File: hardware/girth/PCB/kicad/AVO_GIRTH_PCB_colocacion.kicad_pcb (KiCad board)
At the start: 4 copper layers, 65.5 x 43.5 mm, 122 parts, among them J1 USB-C 16P, J2 BATERÍA 1S, K1 G6KU-2F-Y DC3, Q1 AO3401A, Q10 AO3401A, Q11 AO3400A, Q12 2N7002, Q13 AO3400A, Q14 AO3401A, Q15 2N7002, Q16 2N7002, Q17 AO3401A, Q18 2N7002, Q2 AO3401A, Q3 AO3401A, SW1 REED (1), SW2 REED (2), U1 BQ51013BRHLR, U2 BQ24072RGTR, U3 RT9080-33GJ5, U4 ESP32-C6-MINI-1U-N4, U5 BNO085, U6 USBLC6-2SC6, Y1 32,768 kHz 12,5 pF

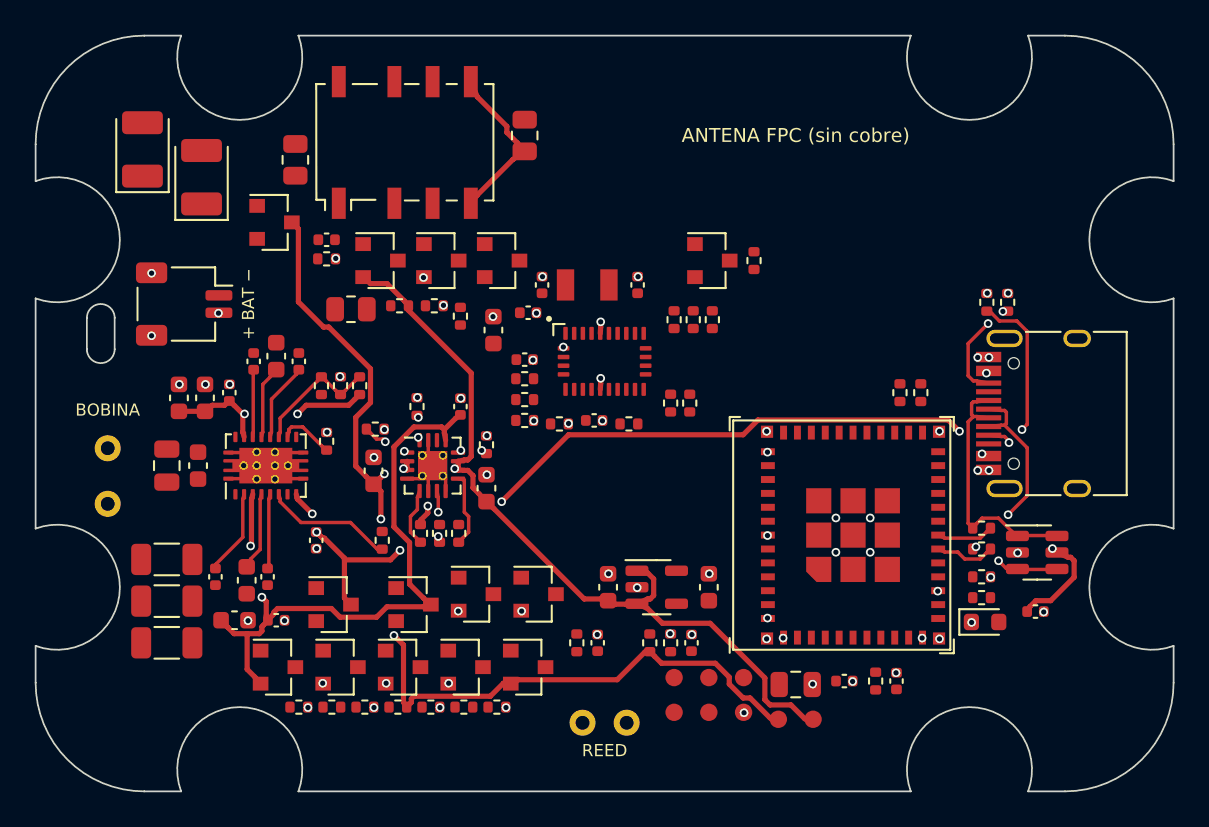
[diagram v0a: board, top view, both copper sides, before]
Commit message: PCB cincha REV B: ESP32-C3-MINI-1U-N4, LSM6DS3TR-C + MMC5983MA por I²C, corte de batería con MOSFET; REV A (C6) congelada
- REV A copiada tal cual a hardware/girth/PCB_REV_A_C6 (puerta superada en e9e5166).
- U4 ESP32-C3-MINI-1U-N4 (C2911374, 1191 uds. en JLCPCB el 2026-10-29); nueva asignación de GPIO.
- IMU: BNO085 (19,50 US$, 80 uds.) sustituido por LSM6DS3TR-C + MMC5983MA (I²C), mismos datos de 9 ejes.
- Relé biestable sustituido por enclavamiento PMOS/NMOS (reed por flanco, 5 V de carga, PWR_HOLD).
- R6/R7 a 3k3 (piezas Basic). Ficheros de fabricación con nombres C3.

Co-Authored-By: Claude Opus 5.5 <noreply@anthropic.com>
Claude-Session: https://claude.ai/code/session_01CHDvF8BfHwPLkrFs9S3ECm
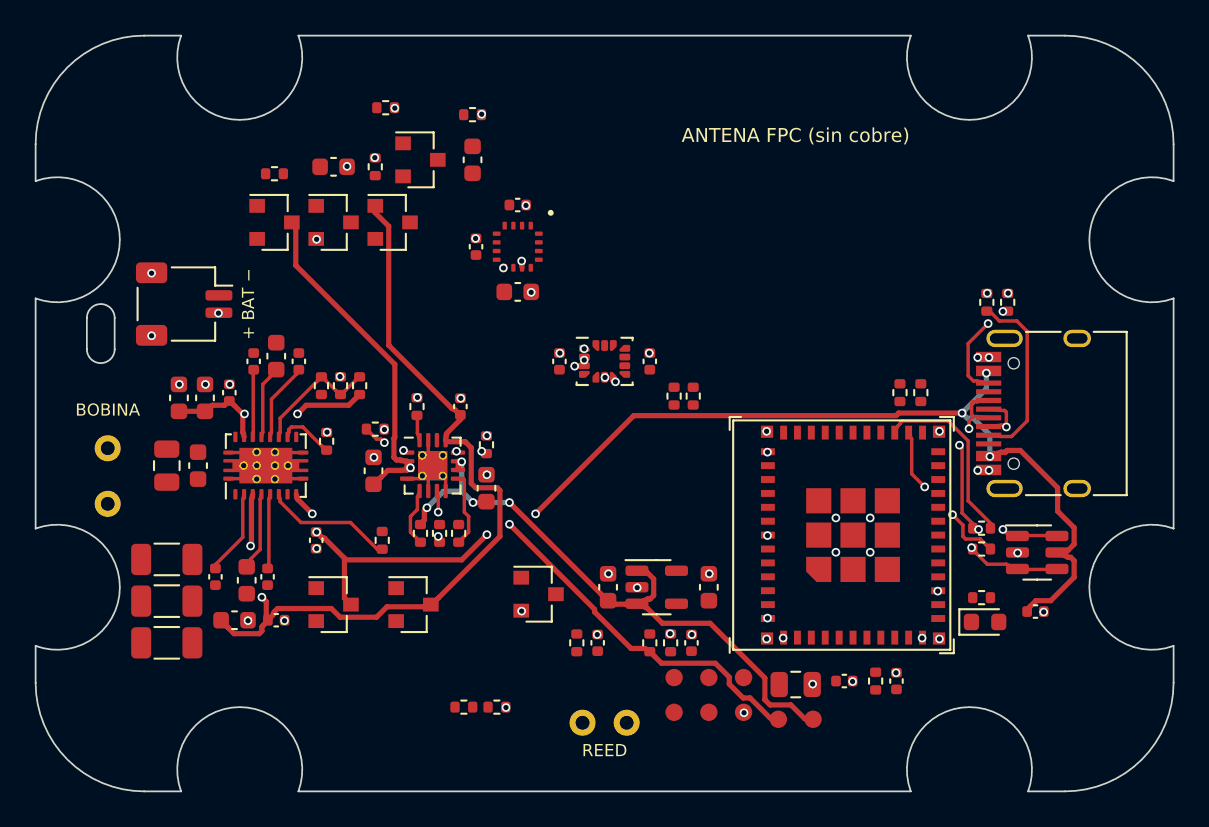
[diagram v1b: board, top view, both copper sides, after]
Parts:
- removed C32, C43: 100n, AVO:C_0402_1005Metric
- removed K1: G6KU-2F-Y DC3, AVO:Relay_DPDT_Omron_G6K-2F-Y
- removed Q12, Q15, Q18: 2N7002, AVO:SOT-23
- removed Q13: AO3400A, AVO:SOT-23
- removed Q14, Q17, Q3: AO3401A, AVO:SOT-23
- removed R14, R22, R23, R24, R25, R26, R27, R44, R45: 10k, AVO:R_0402_1005Metric
- removed R28, R29: 4k7, AVO:R_0402_1005Metric
- removed R30, R46, R47, R48, R53, R54: 100k, AVO:R_0402_1005Metric
- removed R51: 1M, AVO:R_0402_1005Metric
- removed R52: 10R, AVO:R_0805_2012Metric
- removed R55: 1k, AVO:R_0402_1005Metric
- removed Y1: 32,768 kHz 12,5 pF, AVO:Crystal_SMD_3215-2Pin_3.2x1.5mm
- added R42: 1M, AVO:R_0402_1005Metric, F.Cu at (86.8, 85.8)
- added R43: 100k, AVO:R_0402_1005Metric, F.Cu at (87.4, 82.4)
- added U7: MMC5983MA, AVO:MEMSIC_MMC5983MA_LGA-16_3x3mm_P0.5mm, F.Cu at (95.0, 90.4)
- C27, C28: value 22p -> 100n
- C29: value 100n -> 1u
- C30: value 100n -> 10u 6V3; footprint AVO:C_0402_1005Metric -> AVO:C_0603_1608Metric
- C31: value 4u7 -> 100n; footprint AVO:C_0603_1608Metric -> AVO:C_0402_1005Metric
- C40: value 220u 6V3 polímero -> 10u 6V3; footprint AVO:CP_EIA-3528-21_Kemet-B -> AVO:C_0603_1608Metric
- C41: value 220u 6V3 polímero -> 2u2; footprint AVO:CP_EIA-3528-21_Kemet-B -> AVO:C_0603_1608Metric
- D1: value LED verde -> LED rojo
- D10, D11: value BAT54C -> BAV70
- R20, R21: value 10k -> 4k7
- R40, R41: value 0R -> 1M; footprint AVO:R_0805_2012Metric -> AVO:R_0402_1005Metric
- R6: value 3k6 -> 3k3
- R7: value 3k4 -> 3k3
- U4: value ESP32-C6-MINI-1U-N4 -> ESP32-C3-MINI-1U-N4; footprint AVO:ESP32-C6-MINI-1U -> AVO:ESP32-C3-MINI-1U
- U5: value BNO085 -> LSM6DS3TR-C; footprint AVO:CEVA_BNO08x_LGA-28_5.2x3.8mm_P0.5mm -> AVO:LGA-14_3x2.5mm_P0.5mm_LayoutBorder3x4y
- moved D10 26.4 mm to (87.8, 89.0)
- moved Q11 25.6 mm to (84.4, 89.0)
- moved C40 15.6 mm to (92.4, 85.4)
- moved R40 14.6 mm to (81.0, 86.2), turned to 0 degrees
- moved C41 11.0 mm to (84.4, 85.8), turned to 0 degrees
- moved R41 10.5 mm to (92.4, 82.8), turned to 0 degrees
- moved R21 9.70 mm to (105.1, 99.0), turned to 90 degrees
- moved R20 8.66 mm to (104.0, 99.0), turned to 90 degrees
- moved D11 7.47 mm to (89.4, 85.4)
- moved C31 7.33 mm to (95.0, 88.0), turned to 0 degrees
- moved C29 7.08 mm to (92.6, 90.4), turned to 90 degrees
- moved C27 4.51 mm to (97.4, 97.0)
- moved C28 4.46 mm to (102.6, 97.0)
- moved U4 2.00 mm to (113.6, 107.0)
- moved C30 1.34 mm to (95.0, 93.0)
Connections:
- C27 pad 1: IMU_XIN -> +3V3
- C28 pad 1: IMU_XOUT -> +3V3
- C29 pad 1: IMU_VDD -> +3V3
- C30 pad 1: IMU_VDD -> MAG_CAP
- C31 pad 1: IMU_VDD -> +3V3
- C40 pad 1: RLY_P -> REED_HI
- C40 pad 2: K_A -> REED_PULSE
- C41 pad 1: RLY_P -> PWR_G
- C41 pad 2: K_A -> GND
- D1 pad 1: GND -> LED_K
- D1 pad 2: LED_A -> +3V3
- D10 pad 1: REED_HI -> VIN5
- D10 pad 2: VIN5 -> PWR_HOLD
- D10 pad 3: RLY_P -> PWR_G
- D11 pad 1: RLY_ON_D -> REED_PULSE
- D11 pad 2: unconnected-(D11-A2-Pad2) -> REED_PULSE
- D11 pad 3: RLY_GB -> PWR_G
- Q10 pad 1: SS_G -> PWR_PG
- Q10 pad 2: BAT_SW -> BAT_RAW
- Q11 pad 1: RLY_GB -> PWR_G
- Q11 pad 3: K_B -> PWR_PG
- R13 pad 1: GPIO8 -> LED
- R15 pad 2: LED_A -> LED_K
- R20 pad 1: IMU_BOOTN -> I2C_SDA
- R20 pad 2: IMU_VDD -> +3V3
- R21 pad 1: IMU_PS1 -> I2C_SCL
- R21 pad 2: IMU_VDD -> +3V3
- R40 pad 1: RLY_NO -> BAT_RAW
- R40 pad 2: BAT_SW -> PWR_PG
- R41 pad 1: RLY_NC -> REED_PULSE
- R41 pad 2: BAT_SW -> GND
- U4 pad 10: IMU_PWR_N -> unconnected-(U4-NC-Pad10)
- U4 pad 13: IMU_RST -> REED
- U4 pad 15: REED -> unconnected-(U4-NC-Pad15)
- U4 pad 16: IMU_WAKE -> QI_CHG
- U4 pad 17: USB_DM -> unconnected-(U4-NC-Pad17)
- U4 pad 18: USB_DP -> CHG_PG
- U4 pad 19: RLY_ON -> PWR_HOLD
- U4 pad 20: LED -> I2C_SDA
- U4 pad 21: unconnected-(U4-NC-Pad21) -> I2C_SCL
- U4 pad 22: GPIO8 -> LED
- U4 pad 24: IMU_CS -> unconnected-(U4-NC-Pad24)
- U4 pad 25: IMU_SCK -> unconnected-(U4-NC-Pad25)
- U4 pad 26: IMU_MOSI -> USB_DM
- U4 pad 27: IMU_MISO -> USB_DP
- U4 pad 28: QI_CHG -> unconnected-(U4-NC-Pad28)
- U4 pad 29: RLY_OFF -> unconnected-(U4-NC-Pad29)
- U4 pad 5: BAT_ADC -> CHG_STAT
- U4 pad 6: CHG_PG -> BAT_ADC
- U4 pad 9: CHG_STAT -> unconnected-(U4-NC-Pad9)
- U5 pad 1: unconnected-(U5-NC-Pad1) -> GND
- U5 pad 10: GND -> unconnected-(U5-OCS_Aux-Pad10)
- U5 pad 11: IMU_RST -> unconnected-(U5-SDO_Aux-Pad11)
- U5 pad 12: unconnected-(U5-NC-Pad12) -> +3V3
- U5 pad 13: unconnected-(U5-NC-Pad13) -> I2C_SCL
- U5 pad 14: IMU_INT -> I2C_SDA
- U5 pad 3: IMU_VDD -> GND
- U5 pad 4: IMU_BOOTN -> IMU_INT
- U5 pad 5: IMU_PS1 -> +3V3
- U5 pad 6: IMU_WAKE -> GND
- U5 pad 7: unconnected-(U5-NC-Pad7) -> GND
- U5 pad 8: unconnected-(U5-NC-Pad8) -> +3V3
- U5 pad 9: IMU_CAP -> unconnected-(U5-INT2-Pad9)
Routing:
- net VSYS: track 49.6 -> 36.2 mm, vias 2 -> 4
- net VBAT: track 58.9 -> 47.3 mm, vias 4 -> 2
- net VIN5: track 39.8 -> 51.1 mm
- net RLY_NO: track 9.52 -> 0.00 mm
- net USB_DP: track 3.28 -> 10.7 mm
- net USB_DM: track 3.45 -> 9.12 mm, vias 0 -> 2
- net USB_DM_C: track 16.8 -> 16.2 mm, vias 3 -> 2
- net CC1: track 11.0 -> 10.5 mm, vias 2 -> 0
- net VBUS: track 68.4 -> 68.7 mm, vias 8 -> 7
- net GND: track 10.6 -> 10.4 mm, vias 74 -> 68
- net USB_DP_C: track 14.9 -> 14.7 mm, vias 0 -> 4
- net CHG_ISET: track 1.47 -> 1.45 mm, vias 2 -> 0
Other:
- board text added: "AVO GIRTH · REV B · ESP32-C3 · 2026-10-29"
- board text removed: "AVO GIRTH · REV A · 2026-10-29"

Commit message: PCB cincha REV B: huella LGA-14L propia (0,25 mm entre pads; la genérica dejaba 0,1 mm); zip del firmware sin la carpeta build
Co-Authored-By: Claude Opus 5.5 <noreply@anthropic.com>
Claude-Session: https://claude.ai/code/session_01CHDvF8BfHwPLkrFs9S3ECm
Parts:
- U5: footprint AVO:LGA-14_3x2.5mm_P0.5mm_LayoutBorder3x4y -> AVO:ST_LGA-14L_2.5x3mm_P0.5mm

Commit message: Cincha REV B: SCL en GPIO2 (la hoja del ESP32-C3-MINI-1 pide GPIO2 = 1 al arrancar; el pull-up I²C lo garantiza), CHG_STAT en GPIO7
Co-Authored-By: Claude Opus 5.5 <noreply@anthropic.com>
Claude-Session: https://claude.ai/code/session_01CHDvF8BfHwPLkrFs9S3ECm
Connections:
- U4 pad 21: I2C_SCL -> CHG_STAT
- U4 pad 5: CHG_STAT -> I2C_SCL
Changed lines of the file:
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@@
 			(size 0.4 0.8)
 			(layers "F.Cu" "F.Paste" "F.Mask")
-			(net 17 "CHG_STAT")
+			(net 20 "I2C_SCL")
 		)
 		(pad
@@
 			(size 0.4 0.8)
 			(layers "F.Cu" "F.Paste" "F.Mask")
-			(net 20 "I2C_SCL")
+			(net 17 "CHG_STAT")
 		)
 		(pad

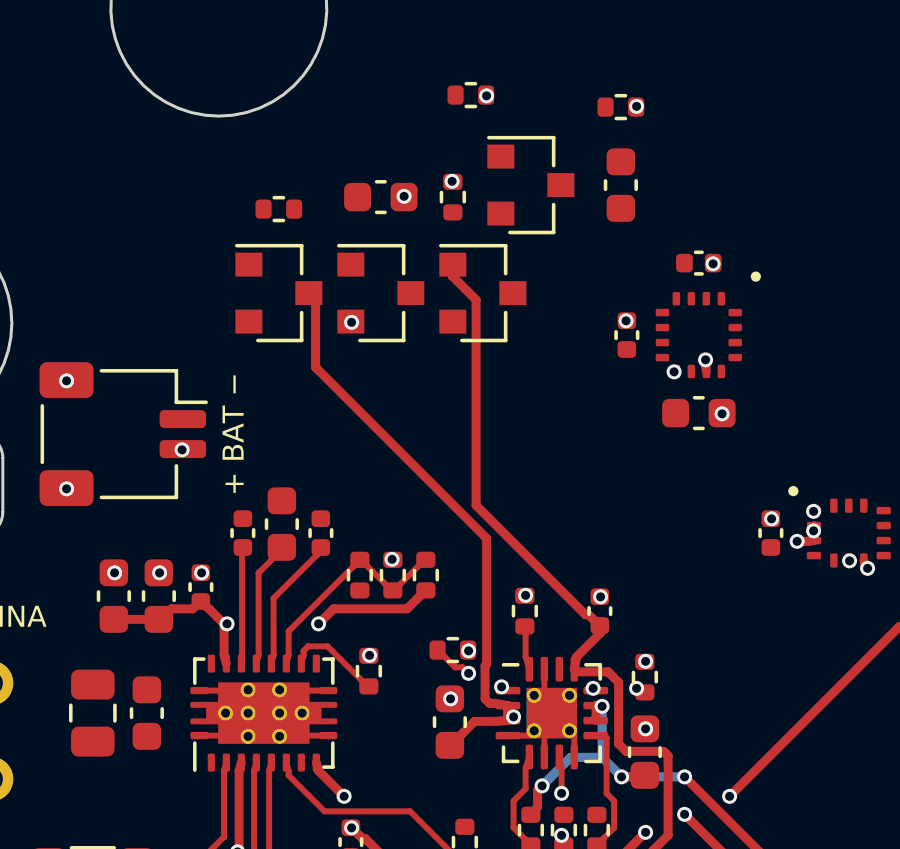
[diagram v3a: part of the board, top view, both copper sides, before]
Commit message: Cincha REV B: red del reed revisada (D12 aísla la lectura, R44 limita la corriente, R45/D13 rearman en ~2 s, C40/C41 10× menores) y firmware: no despertar por reed ya cerrado, IMU al ritmo del dato listo, magnetómetro opcional
Corrige los fallos de una revisión independiente: con el reed cerrado la placa no se podía apagar (despertar por
nivel) y tras sacar la cápsula el reed no la volvía a encender durante 10–25 s.

Co-Authored-By: Claude Opus 5.5 <noreply@anthropic.com>
Claude-Session: https://claude.ai/code/session_01CHDvF8BfHwPLkrFs9S3ECm
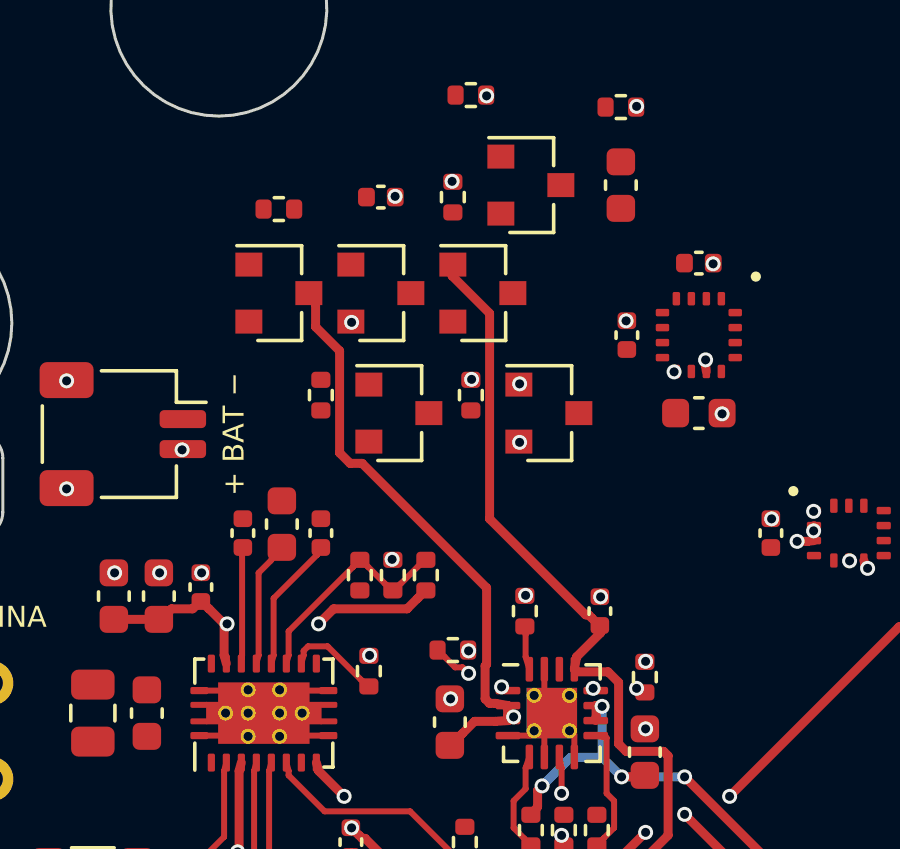
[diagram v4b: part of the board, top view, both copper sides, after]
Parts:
- added D12: BAV70, AVO:SOT-23, F.Cu at (85.0, 93.0)
- added D13: BAV70, AVO:SOT-23, F.Cu at (90.0, 93.0)
- added R44: 220R, AVO:R_0402_1005Metric, F.Cu at (82.4, 92.4)
- added R45: 1M, AVO:R_0402_1005Metric, F.Cu at (87.4, 92.4)
- C40: value 10u 6V3 -> 2u2
- C41: value 2u2 -> 220n; footprint AVO:C_0603_1608Metric -> AVO:C_0402_1005Metric
- R41, R42: value 1M -> 10M
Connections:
- C40 pad 1: REED_HI -> REED_CR
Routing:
- net GND: track 10.4 -> 10.5 mm, vias 68 -> 71
